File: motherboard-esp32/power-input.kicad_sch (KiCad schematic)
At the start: 16 parts, among them J3 JST_2P_XH, J4 JST_2P_XH, J7 XT60, Q1 DOD4185, Q2 DOD4185, Q3 HL3415A, Q4 HL3415A

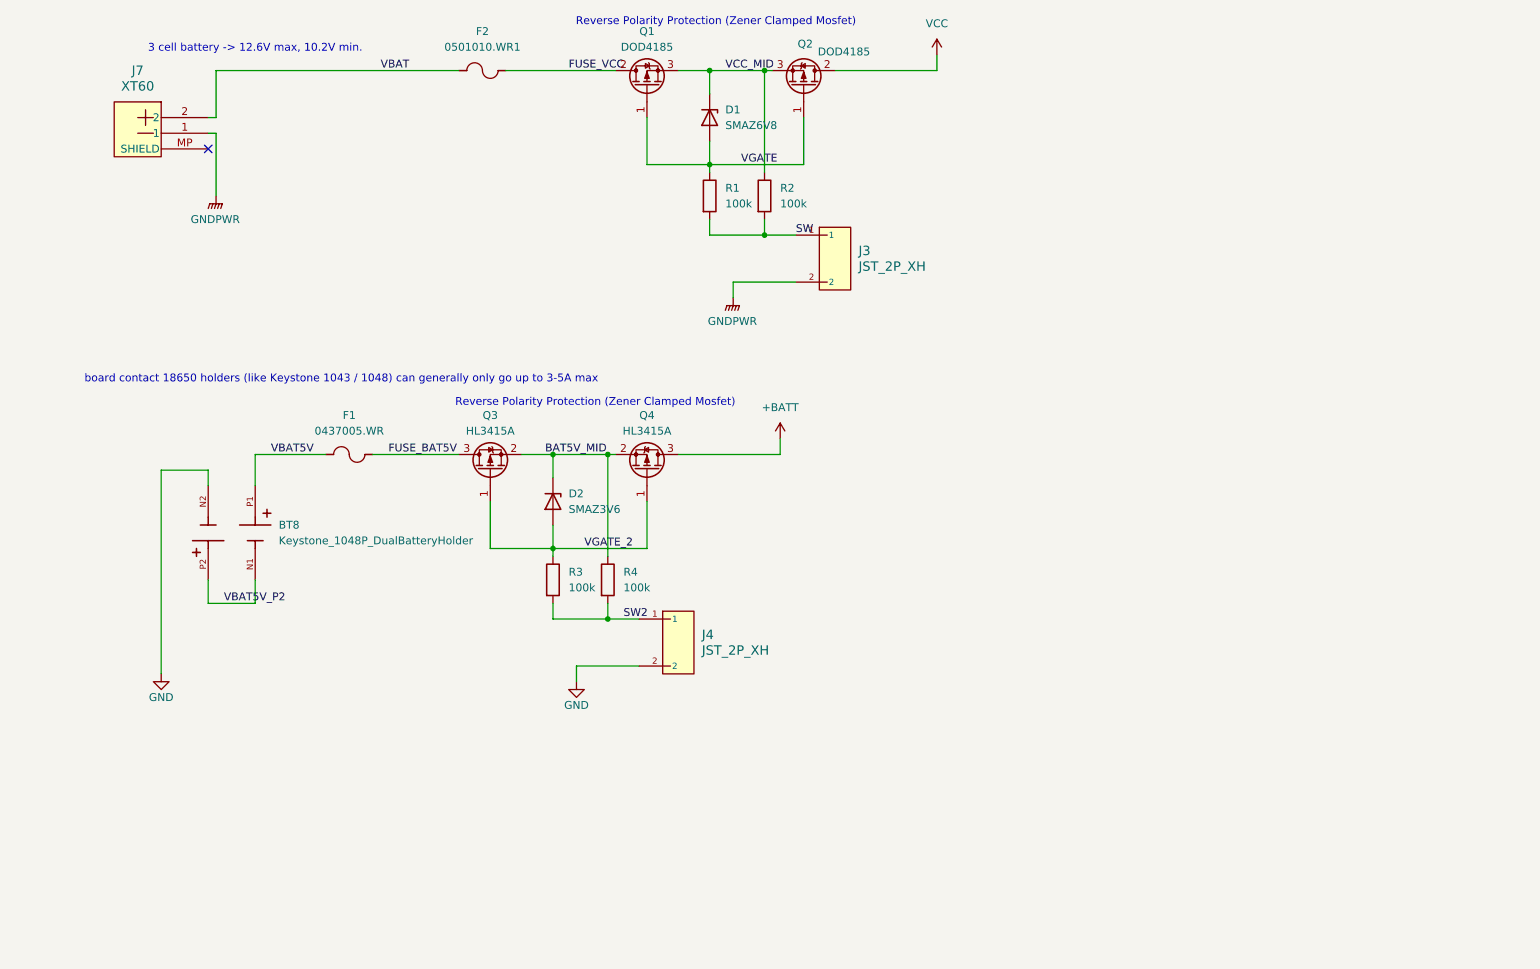
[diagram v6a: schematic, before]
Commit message: 5V 5A version
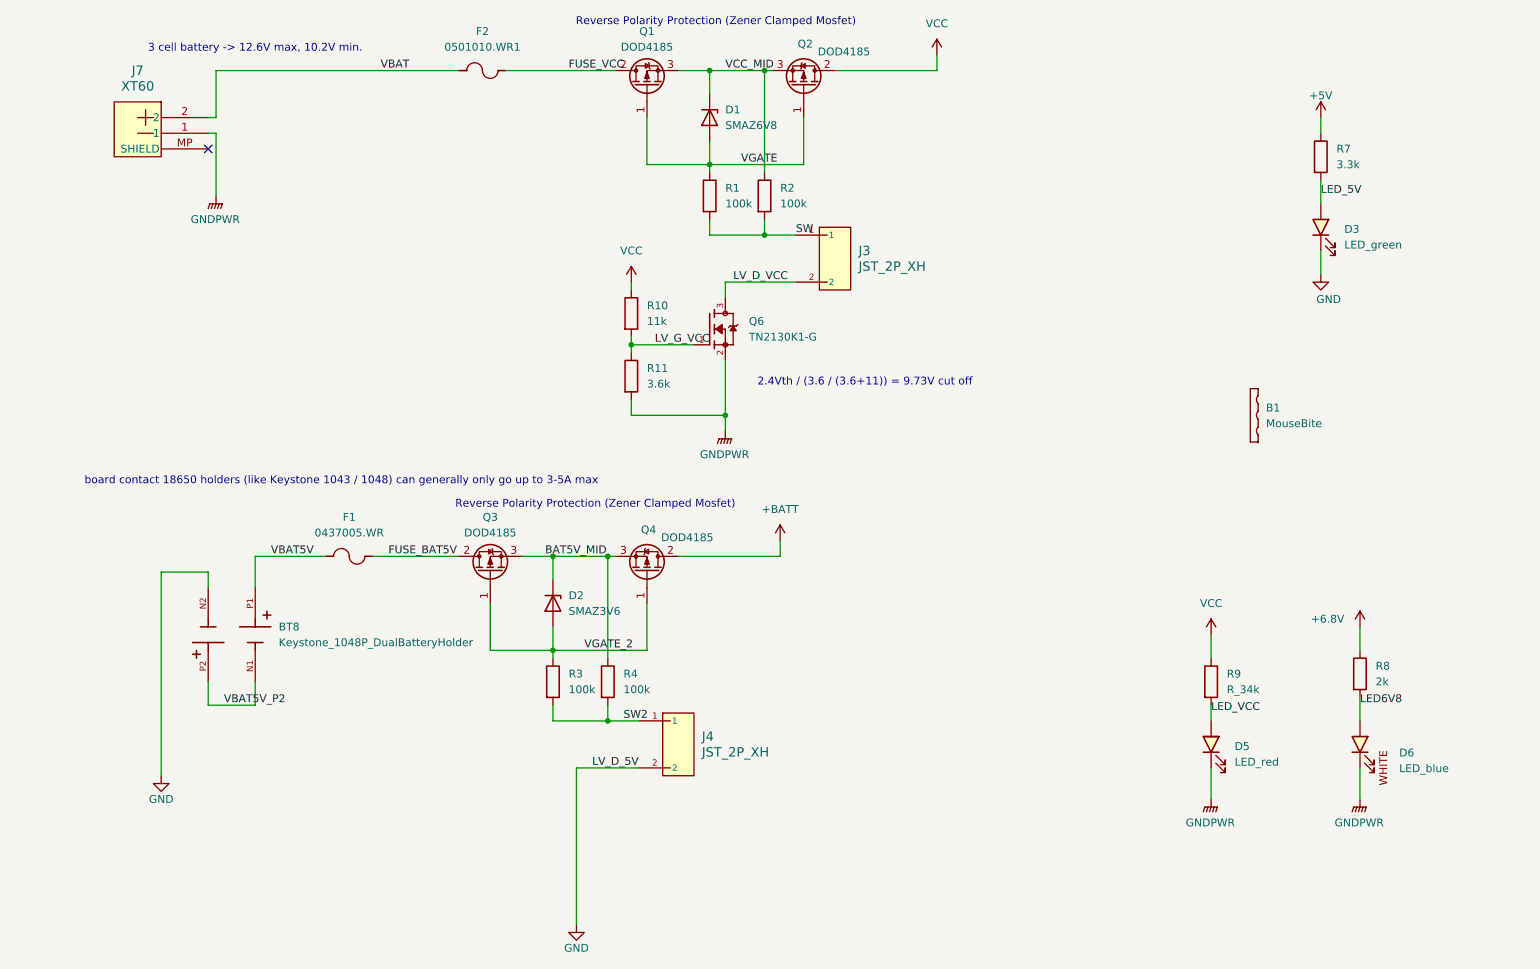
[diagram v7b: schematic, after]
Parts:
- removed Q3, Q4: HL3415A, bio-robot:SOT-23, symbol bio-robot:Q_Pch20V5.6A
- added B1: MouseBite, bio-robot:MouseBite-Long, symbol Mechanical:MouseBite
- added D3: LED_green, bio-robot:LED_0805_2012Metric, symbol bio-robot:LED_green
- added D5: LED_red, bio-robot:LED_0805_2012Metric, symbol bio-robot:LED_red
- added D6: LED_blue, bio-robot:LED_0603_1608Metric, symbol bio-robot:LED_white
- added Q3, Q4: DOD4185, bots:DPAK-3_ONS, symbol bio-robot:Q_Pch40V45A
- added Q6: TN2130K1-G, bio-robot:SOT95P240X111-3N, symbol bio-robot:Q_TN2130K1-G
- added R10: 11k, bio-robot:R_0603_1608Metric, symbol bio-robot:R_11k
- added R11: 3.6k, bio-robot:R_0603_1608Metric, symbol bio-robot:R_3.6k
- added R7: 3.3k, bio-robot:R_0603_1608Metric, symbol bio-robot:R_3.3k
- added R8: 2k, bio-robot:R_0603_1608Metric, symbol bio-robot:R_2k
- added R9: R_34k, bio-robot:R_0603_1608Metric, symbol bio-robot:R_34k
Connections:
- net +BATT: now also Q4.2 (D)
- net BAT5V_MID: now also Q3.3 (S), Q4.3 (S)
- net FUSE_BAT5V: now also Q3.2 (D)
- net GND: now also D3.1 (K)
- net GNDPWR: now also D5.1 (K), D6.1 (K), Q6.2, R11.2; no longer J3.2
- net VCC: now also R10.1, R9.1
- net VGATE_2: now also Q3.1 (G), Q4.1 (G)
- new net +5V: R7.1
- new net +6.8V: R8.1
- new net LED6V8: D6.2 (A), R8.2
- new net LED_5V: D3.2 (A), R7.2
- new net LED_VCC: D5.2 (A), R9.2
- new net LV_D_VCC: J3.2, Q6.3
- new net LV_G_VCC: Q6.1, R10.2, R11.1
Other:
- note added: "2.4Vth / (3.6 / (3.6+11)) = 9.73V cut off"
- moved on the sheet: BT8, D2, F1, J4, R3, R4

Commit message: ordered
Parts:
- B1: value MouseBite -> Long_4mm_Attachment_no_mousebites; footprint bio-robot:MouseBite-Long -> bio-robot:Long_4mm_attachment_no_mouse_bites; symbol Mechanical:MouseBite -> bio-robot:Long_Attachment_no_mousebites
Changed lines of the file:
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@@
 	)
 	(symbol
-		(lib_id "Mechanical:MouseBite")
+		(lib_id "bio-robot:Long_Attachment_no_mousebites")
 		(at 210.82 85.09 0)
 		(unit 1)
@@
 			)
 		)
-		(property "Value" "MouseBite"
+		(property "Value" "Long_4mm_Attachment_no_mousebites"
 			(at 213.36 86.4224 0)
 			(show_name no)
@@
 			)
 		)
-		(property "Footprint" "bio-robot:MouseBite-Long"
+		(property "Footprint" "bio-robot:Long_4mm_attachment_no_mouse_bites"
 			(at 210.82 85.09 0)
 			(hide yes)
